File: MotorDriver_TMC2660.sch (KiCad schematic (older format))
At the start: 17 parts, among them U4 TMC2660

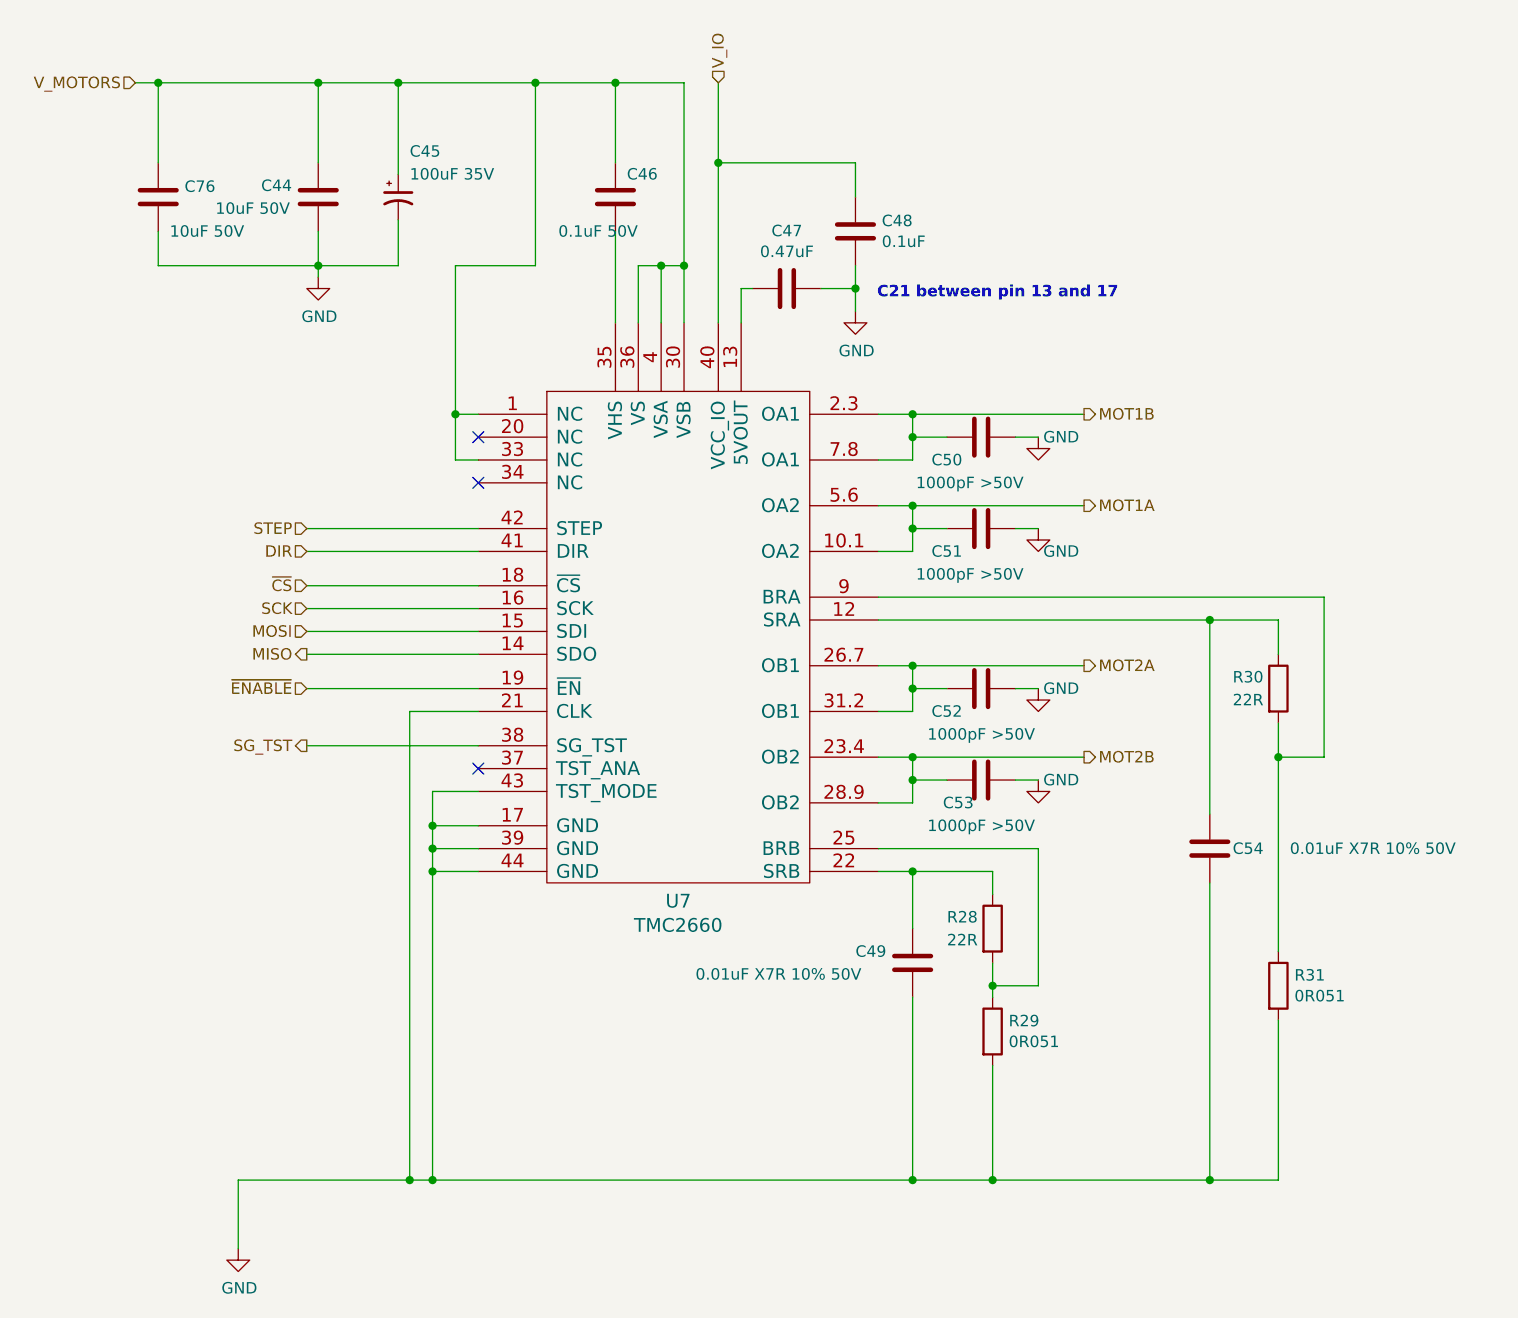
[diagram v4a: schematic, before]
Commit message: Reset schematics for tmc2660. Clean the board layout.
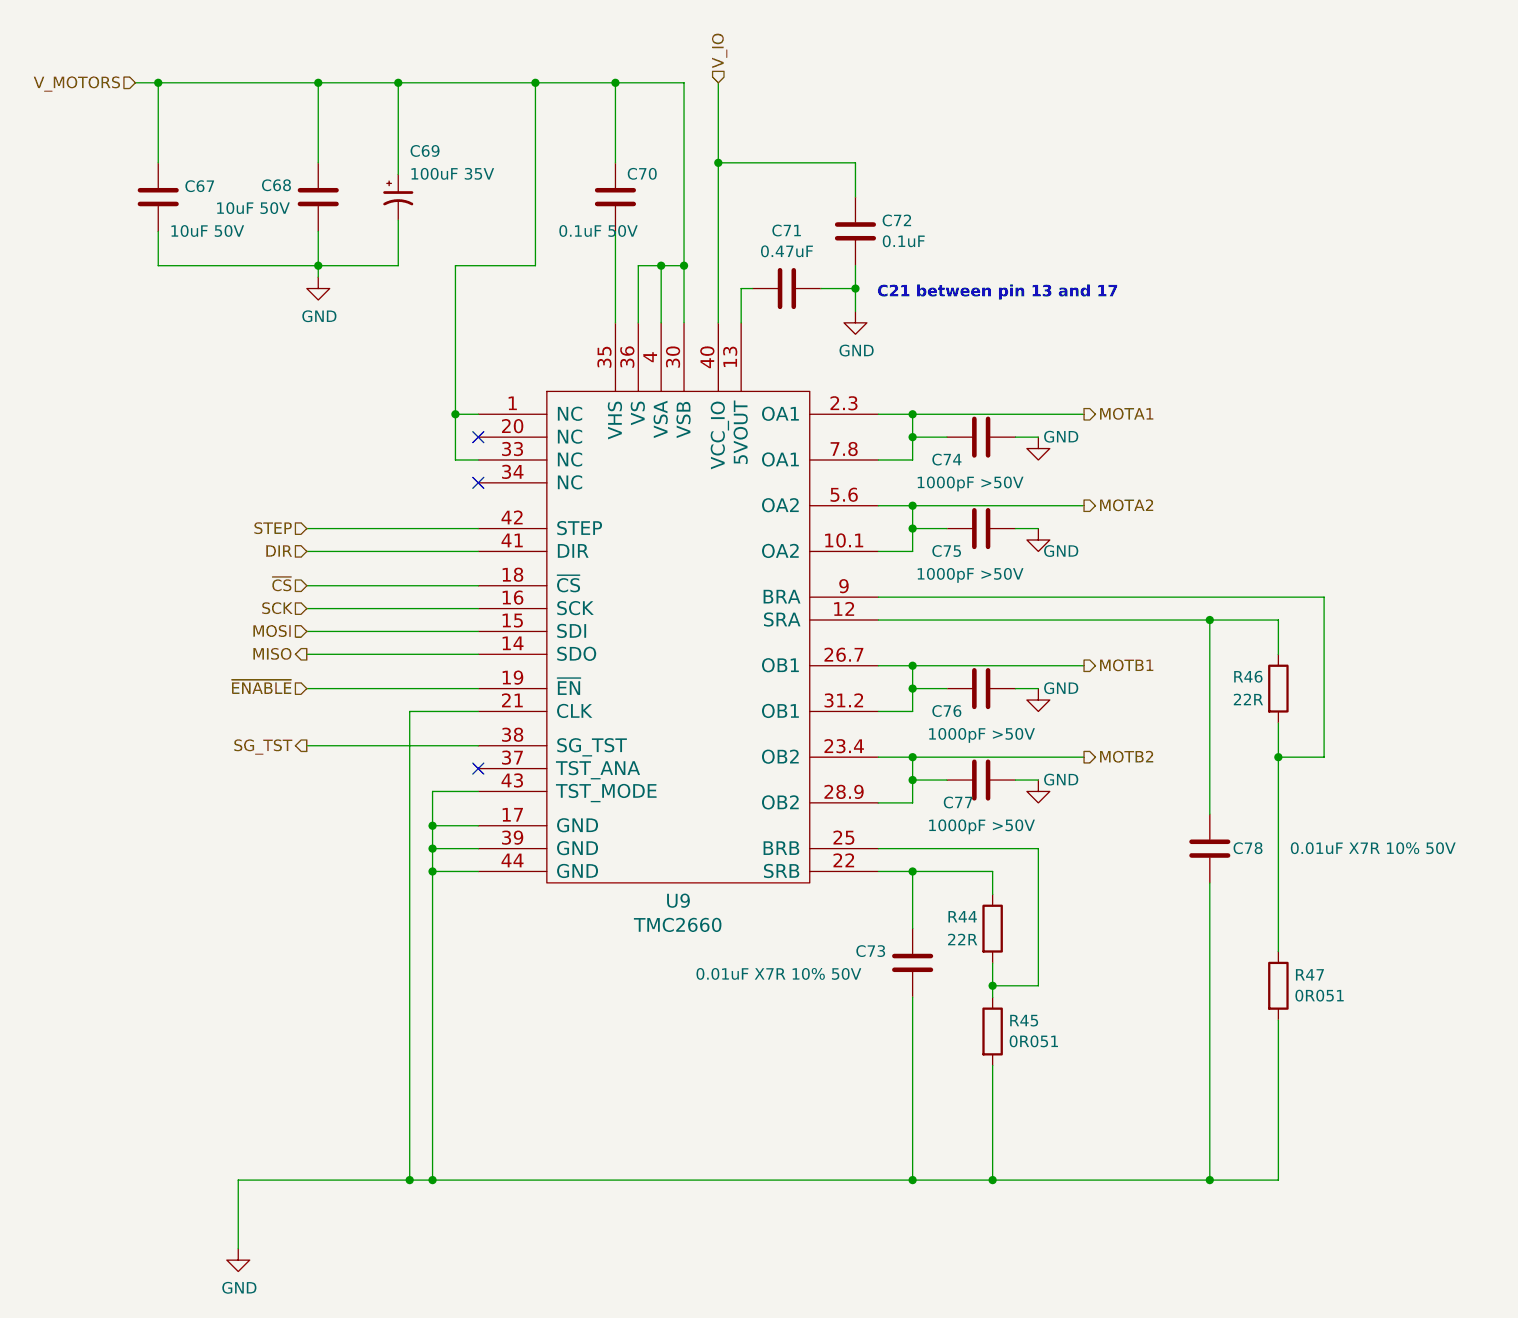
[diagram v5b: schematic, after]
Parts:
- renumbered C4 to C11, C5 to C12, C6 to C13, C7 to C14, C8 to C15, C9 to C16, C10 to C17, C11 to C18, C12 to C19, C13 to C20, C14 to C21, C74 to C25, R2 to R10, R3 to R11, R4 to R12, R5 to R13, U4 to U5
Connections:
- net MOT1A renamed MOTA2
- net MOT1B renamed MOTA1
- net MOT2A renamed MOTB1
- net MOT2B renamed MOTB2

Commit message: Updated component values, updated component footprint.
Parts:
- C13: footprint PrntrBoardV1:C_0603_1608Metric -> PrntrBoardV1:C_0402_1005Metric
- C16, C21: value 0.01uF X7R 10% 50V -> 0.01uF
- C17, C18, C19, C20: value 1000pF >50V -> 1000pF
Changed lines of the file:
@@
 $Descr A4 11693 8268
 encoding utf-8
-Sheet 9 35
+Sheet 26 35
 Title ""
 Date ""
@@
 F 0 "C70" H 4650 1800 50  0000 L CNN
 F 1 "0.1uF 50V" H 4350 1550 50  0000 L CNN
-F 2 "PrntrBoardV1:C_0603_1608Metric" H 4638 1550 50  0001 C CNN
+F 2 "PrntrBoardV1:C_0402_1005Metric" H 4638 1550 50  0001 C CNN
 F 3 "~" H 4600 1700 50  0001 C CNN
 	1    4600 1700
@@
 AR Path="/5AC337B6/5AD9F95A/5AD4B0F5/5AC33CA1" Ref="C74"  Part="1"
 F 0 "C74" V 6300 2600 50  0000 C CNN
-F 1 "1000pF >50V" V 6400 2700 50  0000 C CNN
+F 1 "1000pF" V 6400 2700 50  0000 C CNN
 F 2 "PrntrBoardV1:C_0603_1608Metric" H 6238 2600 50  0001 C CNN
 F 3 "~" H 6200 2750 50  0001 C CNN
@@
 AR Path="/5AC337B6/5AD9F95A/5AD4B0F5/5AC33D6E" Ref="C75"  Part="1"
 F 0 "C75" V 6300 3000 50  0000 C CNN
-F 1 "1000pF >50V" V 6400 3100 50  0000 C CNN
+F 1 "1000pF" V 6400 3100 50  0000 C CNN
 F 2 "PrntrBoardV1:C_0603_1608Metric" H 6238 3000 50  0001 C CNN
 F 3 "~" H 6200 3150 50  0001 C CNN
@@
 AR Path="/5AC337B6/5AD9F95A/5AD4B0F5/5AC33DC1" Ref="C76"  Part="1"
 F 0 "C76" V 6300 3700 50  0000 C CNN
-F 1 "1000pF >50V" V 6400 3850 50  0000 C CNN
+F 1 "1000pF" V 6400 3850 50  0000 C CNN
 F 2 "PrntrBoardV1:C_0603_1608Metric" H 6238 3700 50  0001 C CNN
 F 3 "~" H 6200 3850 50  0001 C CNN
@@
 AR Path="/5AC337B6/5AD9F95A/5AD4B0F5/5AC33E6E" Ref="C77"  Part="1"
 F 0 "C77" V 6300 4150 50  0000 C CNN
-F 1 "1000pF >50V" V 6400 4250 50  0000 C CNN
+F 1 "1000pF" V 6400 4250 50  0000 C CNN
 F 2 "PrntrBoardV1:C_0603_1608Metric" H 6238 4100 50  0001 C CNN
 F 3 "~" H 6200 4250 50  0001 C CNN
@@
 AR Path="/5AC337B6/5ACE1C6D/5ACC0B66/5AC33EDF" Ref="C64"  Part="1"
 AR Path="/5AC337B6/5AD9F95A/5AD4B0F5/5AC33EDF" Ref="C78"  Part="1"
-F 0 "C78" H 7300 4550 50  0000 L CNN
-F 1 "0.01uF X7R 10% 50V" H 7550 4550 50  0000 L CNN
+F 0 "C78" H 6900 4550 50  0000 L CNN
+F 1 "0.01uF" H 6850 4400 50  0000 L CNN
 F 2 "PrntrBoardV1:C_0603_1608Metric" H 7238 4400 50  0001 C CNN
 F 3 "~" H 7200 4550 50  0001 C CNN
@@
 AR Path="/5AC337B6/5AD9F95A/5AD4B0F5/5AC33F7D" Ref="C73"  Part="1"
 F 0 "C73" H 5650 5100 50  0000 L CNN
-F 1 "0.01uF X7R 10% 50V" H 4950 5000 50  0000 L CNN
+F 1 "0.01uF" H 5400 5000 50  0000 L CNN
 F 2 "PrntrBoardV1:C_0603_1608Metric" H 5938 4900 50  0001 C CNN
 F 3 "~" H 5900 5050 50  0001 C CNN

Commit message: Added clock source for the TMC2660 drivers.
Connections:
- net GND: no longer U5.21 (CLK)
- new net CLOCK: U5.21 (CLK)
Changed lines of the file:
@@
 $Descr A4 11693 8268
 encoding utf-8
-Sheet 26 35
+Sheet 9 35
 Title ""
 Date ""
@@
 	3800 4450 3800 4550
 Wire Wire Line
-	3800 6000 3700 6000
-Wire Wire Line
 	4000 4550 3800 4550
 Connection ~ 3800 4550
@@
 	3800 4300 3800 4450
 Connection ~ 3800 4450
-Wire Wire Line
-	4000 3950 3700 3950
-Wire Wire Line
-	3700 3950 3700 6000
-Connection ~ 3700 6000
 Wire Wire Line
 	7500 3700 7500 3550
@@
 	2950 6300 2950 6000
 Wire Wire Line
-	2950 6000 3700 6000
-Wire Wire Line
 	6350 3150 6450 3150
 $Comp
@@
 Wire Wire Line
 	2600 2000 3300 2000
+Wire Wire Line
+	2950 6000 3800 6000
+Text HLabel 3250 3950 0    50   Input ~ 0
+CLOCK
+Wire Wire Line
+	3250 3950 4000 3950
 $EndSCHEMATC
